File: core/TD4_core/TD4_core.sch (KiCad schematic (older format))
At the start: 0 parts

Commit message: Started refactoring
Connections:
- net labels removed: CLK, nRESET
- wire segments 61 -> 9

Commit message: RAM refactoring goes on
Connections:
- net labels added: GND, VCC
- net labels removed: 0, 1, 2, 3
- wire segments 9 -> 3
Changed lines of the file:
@@
 $EndDescr
 $Sheet
-S 1650 1200 1350 800
+S 1200 2100 1350 800
 U 5C594EF5
 F0 "Register file" 50
 F1 "register_file.sch" 50
-F2 "A" O R 3000 1300 100
-F3 "B" O R 3000 1500 100
-F4 "OUT" O R 3000 1700 100
-F5 "PC" O R 3000 1900 100
-F6 "Reg_sel" I L 1650 1900 100
-F7 "In" I L 1650 1500 100
+F2 "A" O R 2550 2200 100
+F3 "B" O R 2550 2400 100
+F4 "OUT" O R 2550 2600 100
+F5 "PC" O R 2550 2800 100
+F6 "Reg_sel" I L 1200 2800 100
+F7 "In" I L 1200 2400 100
 $EndSheet
 $Sheet
-S 8450 1900 1150 1750
+S 5950 2300 900  400
 U 5C594F14
 F0 "Adder" 50
 F1 "Adder.sch" 50
-F2 "A_0" I L 8450 2050 101
-F3 "B_0" I L 8450 3050 101
-F4 "A_1" I L 8450 2200 101
-F5 "B_1" I L 8450 3200 101
-F6 "A_2" I L 8450 2350 101
-F7 "B_2" I L 8450 3350 101
-F8 "A_3" I L 8450 2500 101
-F9 "B_3" I L 8450 3500 101
-F10 "Sum_0" I R 9600 2550 101
-F11 "Sum_1" I R 9600 2700 101
-F12 "Sum_2" I R 9600 2850 101
-F13 "Sum_3" I R 9600 3000 101
-F14 "C_out" I R 9600 3300 101
+F2 "C_out" O R 6850 2600 100
+F3 "A" I L 5950 2400 100
+F4 "B" I L 5950 2600 100
+F5 "Q" O R 6850 2400 100
 $EndSheet
 $Sheet
@@
 $EndSheet
 $Sheet
-S 5250 1250 1350 2100
+S 3750 2100 550  800
 U 5C594F9A
 F0 "Multiplexer 4x 4->1" 50
 F1 "Multiplexer_4x_4-1.sch" 50
-F2 "In_A_0" I L 5250 1350 101
-F3 "In_A_1" I L 5250 1500 101
-F4 "In_A_2" I L 5250 1650 101
-F5 "In_A_3" I L 5250 1800 101
-F6 "In_B_0" I L 5250 2050 101
-F7 "In_B_1" I L 5250 2200 101
-F8 "In_B_2" I L 5250 2350 101
-F9 "In_B_3" I L 5250 2500 101
-F10 "In_IN_0" I L 5250 2750 101
-F11 "In_IN_1" I L 5250 2900 101
-F12 "In_IN_2" I L 5250 3050 101
-F13 "In_IN_3" I L 5250 3200 101
-F14 "Sel_0" I R 6600 3050 101
-F15 "Sel_1" I R 6600 3200 101
-F16 "Out_0" I R 6600 2050 101
-F17 "Out_1" I R 6600 2200 101
-F18 "Out_2" I R 6600 2350 101
-F19 "Out_3" I R 6600 2500 101
+F2 "A" I L 3750 2200 100
+F3 "B" I L 3750 2400 100
+F4 "IN" I L 3750 2600 100
+F5 "Sel" I L 3750 2800 100
+F6 "Q" O R 4300 2400 100
 $EndSheet
 $Sheet
-S 8450 3950 1150 300
+S 7150 3150 1150 300
 U 5C5950B1
 F0 "Carry" 50
 F1 "Carry.sch" 50
-F2 "C_in" I L 8450 4100 101
-F5 "nC_out" I R 9600 4100 101
+F2 "C_in" I L 7150 3300 101
+F3 "~C_out" O R 8300 3300 100
 $EndSheet
+Wire Bus Line
+	2550 2200 3750 2200
+Wire Bus Line
+	2550 2400 3750 2400
+Wire Bus Line
+	4300 2400 5950 2400
 Wire Wire Line
-	2300 6300 2000 6300
-Entry Wire Line
-	2000 6300 1900 6400
-Entry Wire Line
-	2000 6450 1900 6550
-Entry Wire Line
-	2000 6600 1900 6700
-Entry Wire Line
-	2000 6750 1900 6850
+	6850 2600 6950 2600
 Wire Wire Line
-	2300 6450 2000 6450
+	6950 2600 6950 3300
 Wire Wire Line
-	2300 6600 2000 6600
-Wire Wire Line
-	2300 6750 2000 6750
-Text Label 2000 6300 0    50   ~ 0
-0
-Text Label 2000 6450 0    50   ~ 0
-1
-Text Label 2000 6600 0    50   ~ 0
-2
-Text Label 2000 6750 0    50   ~ 0
-3
-Wire Wire Line
-	9600 3300 9900 3300
-Wire Wire Line
-	9900 3300 9900 3800
-Wire Wire Line
-	9900 3800 8100 3800
-Wire Wire Line
-	8100 3800 8100 4100
-Wire Wire Line
-	8100 4100 8450 4100
+	6950 3300 7150 3300
+$Comp
+L power:GND #PWR?
+U 1 1 5C6E1765
+P 10600 6200
+F 0 "#PWR?" H 10600 5950 50  0001 C CNN
+F 1 "GND" H 10605 6027 50  0000 C CNN
+F 2 "" H 10600 6200 50  0001 C CNN
+F 3 "" H 10600 6200 50  0001 C CNN
+	1    10600 6200
+	1    0    0    -1
+$EndComp
+$Comp
+L power:VCC #PWR?
+U 1 1 5C6E17B1
+P 10300 6200
+F 0 "#PWR?" H 10300 6050 50  0001 C CNN
+F 1 "VCC" H 10317 6373 50  0000 C CNN
+F 2 "" H 10300 6200 50  0001 C CNN
+F 3 "" H 10300 6200 50  0001 C CNN
+	1    10300 6200
+	1    0    0    -1
+$EndComp
+$Comp
+L power:PWR_FLAG #FLG?
+U 1 1 5C6E17FD
+P 10600 6200
+F 0 "#FLG?" H 10600 6275 50  0001 C CNN
+F 1 "PWR_FLAG" H 10600 6374 50  0000 C CNN
+F 2 "" H 10600 6200 50  0001 C CNN
+F 3 "~" H 10600 6200 50  0001 C CNN
+	1    10600 6200
+	1    0    0    -1
+$EndComp
+$Comp
+L power:PWR_FLAG #FLG?
+U 1 1 5C6E180F
+P 10300 6200
+F 0 "#FLG?" H 10300 6275 50  0001 C CNN
+F 1 "PWR_FLAG" H 10300 6373 50  0000 C CNN
+F 2 "" H 10300 6200 50  0001 C CNN
+F 3 "~" H 10300 6200 50  0001 C CNN
+	1    10300 6200
+	-1   0    0    1
+$EndComp
 $EndSCHEMATC

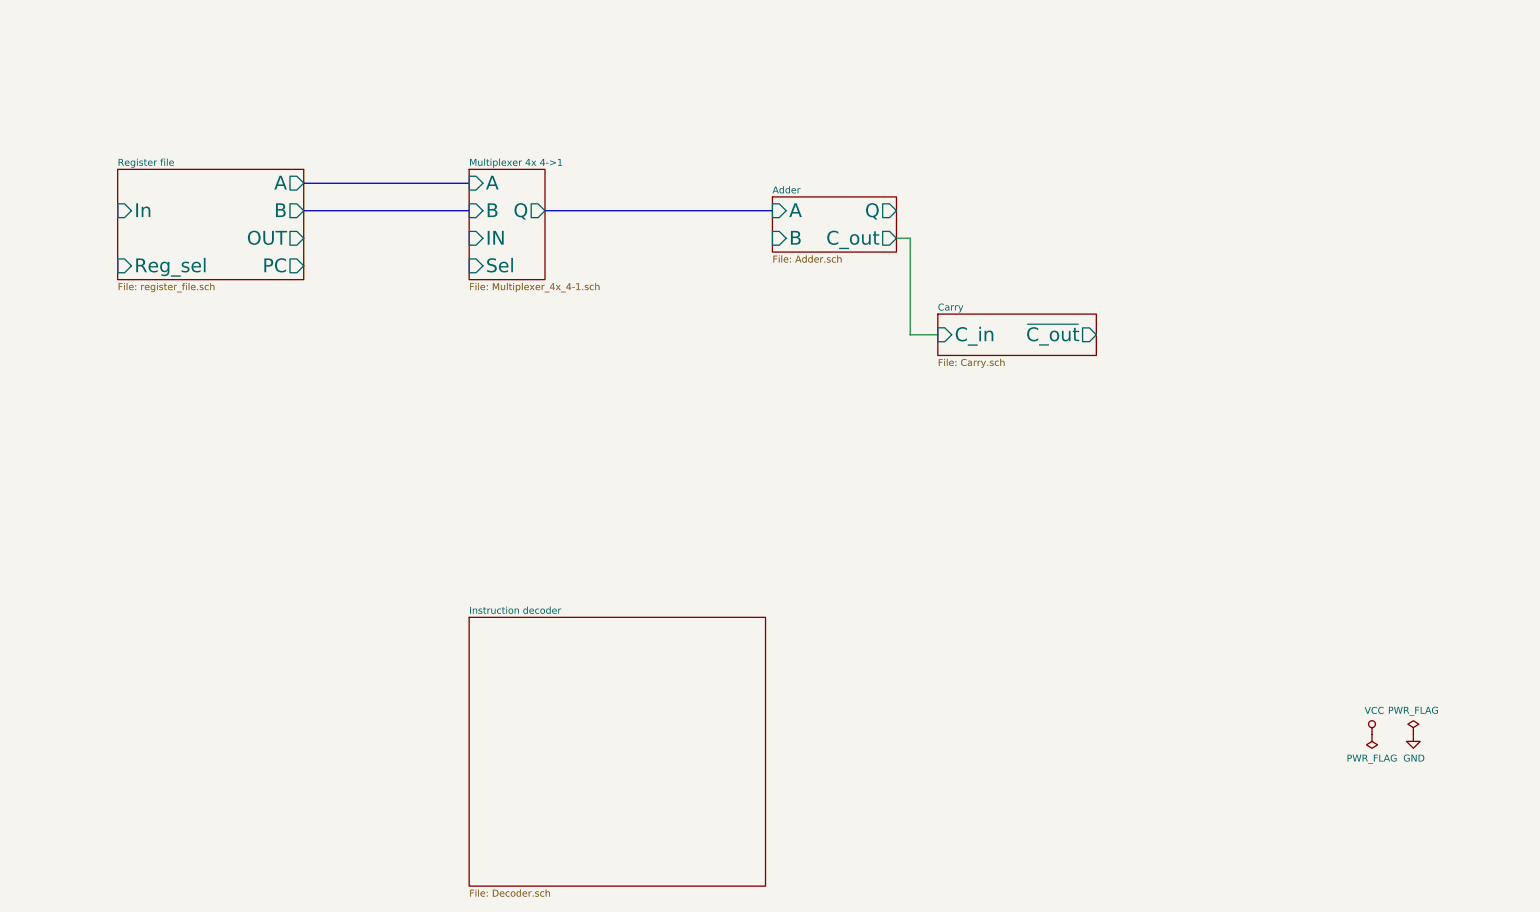
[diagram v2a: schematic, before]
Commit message: Main core schematic done; only decoder left
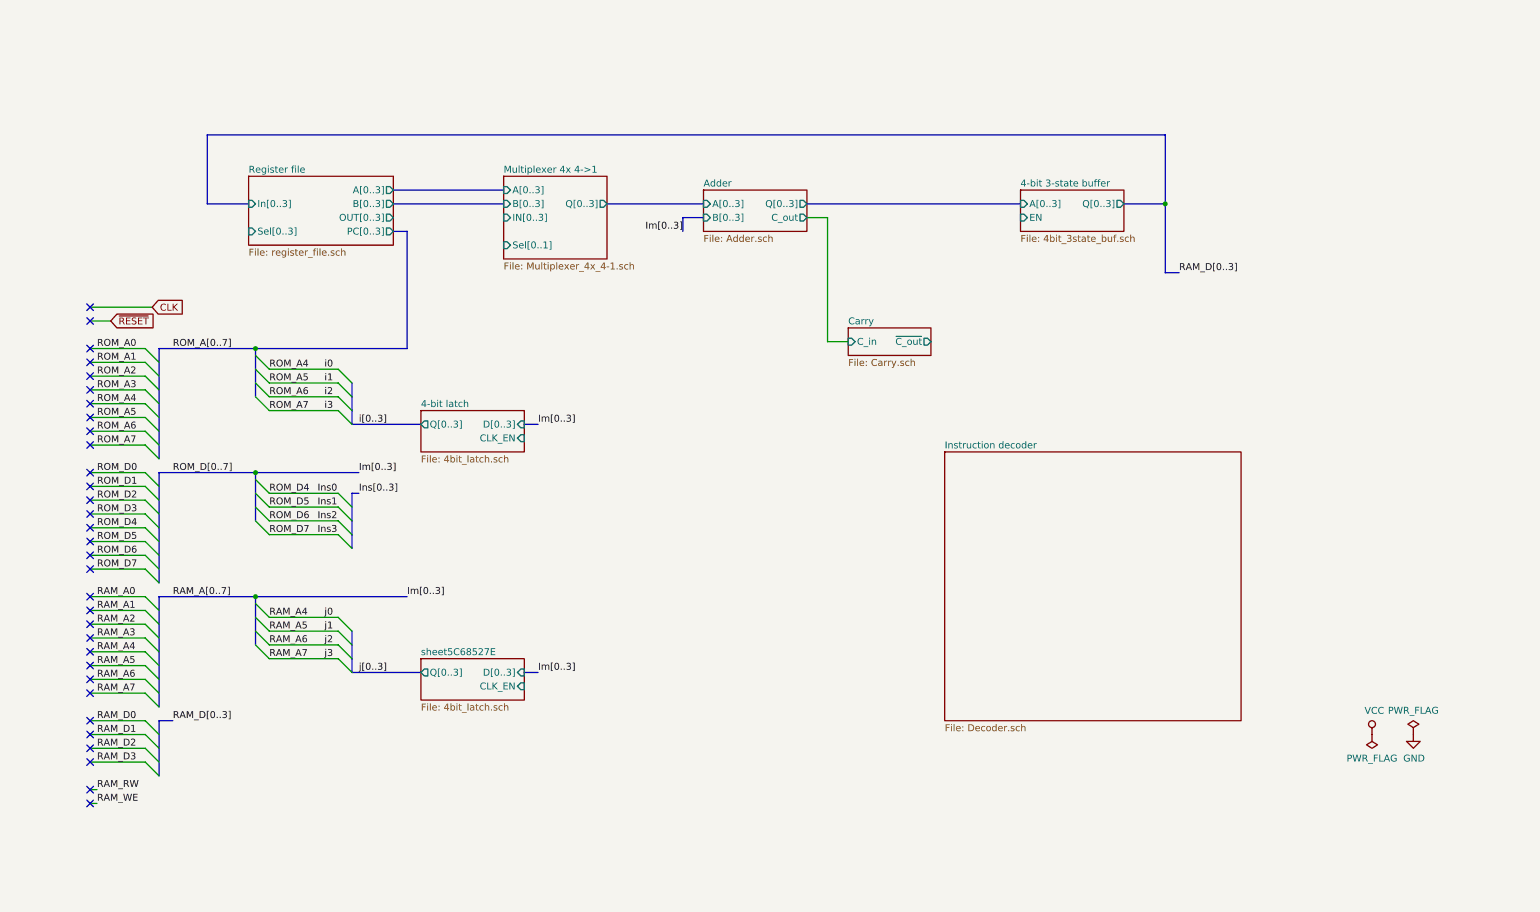
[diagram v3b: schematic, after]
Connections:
- no-connect marks 0 -> 32

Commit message: Core assembled; decoder left
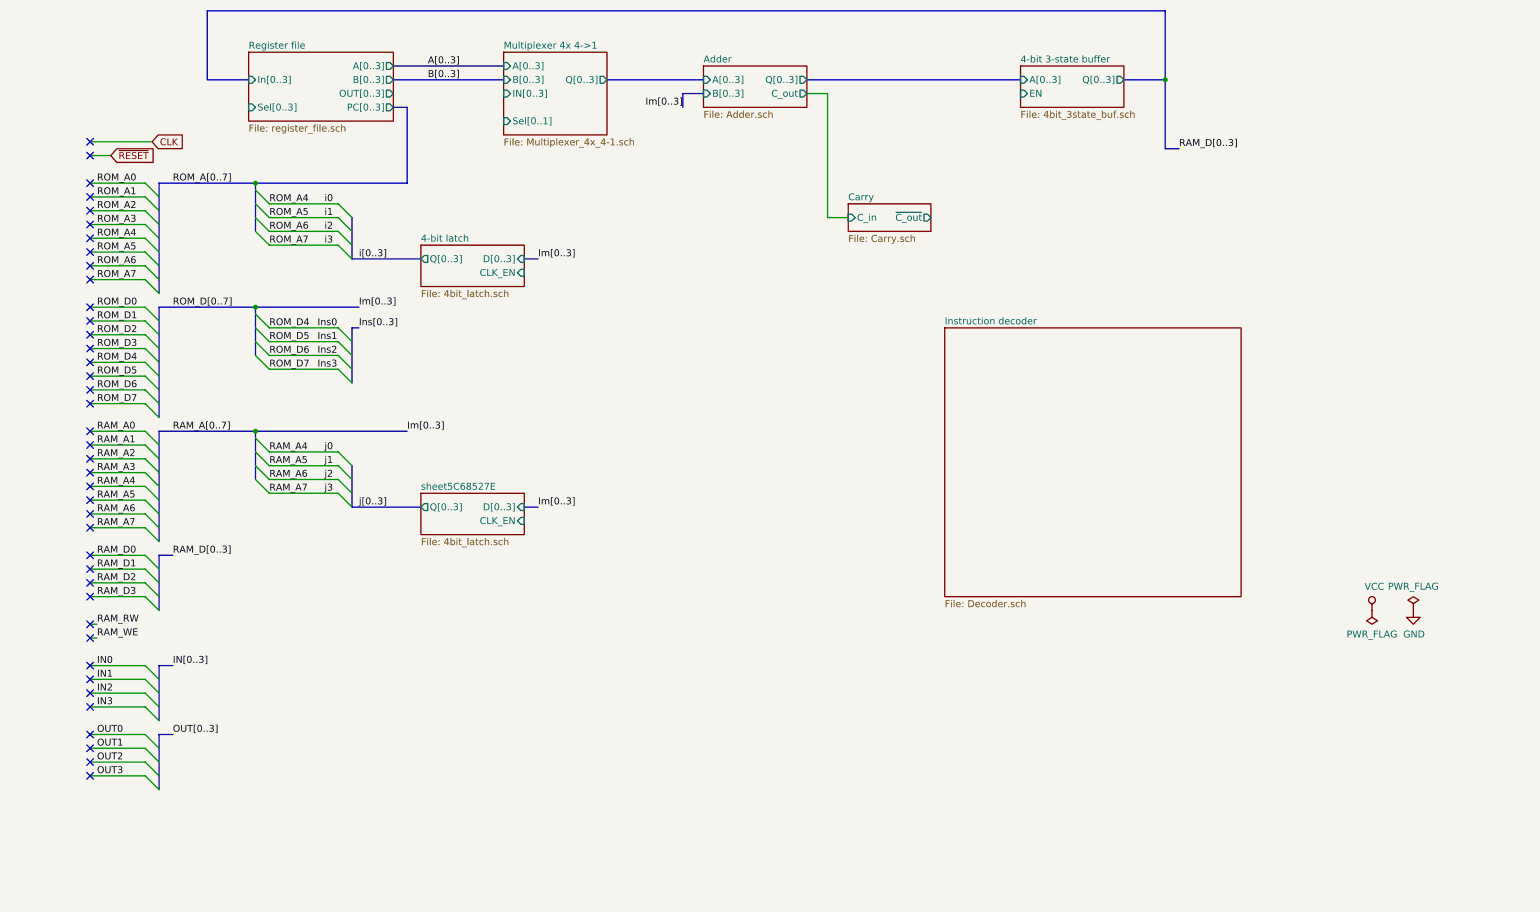
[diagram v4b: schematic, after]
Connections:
- no-connect marks 32 -> 40

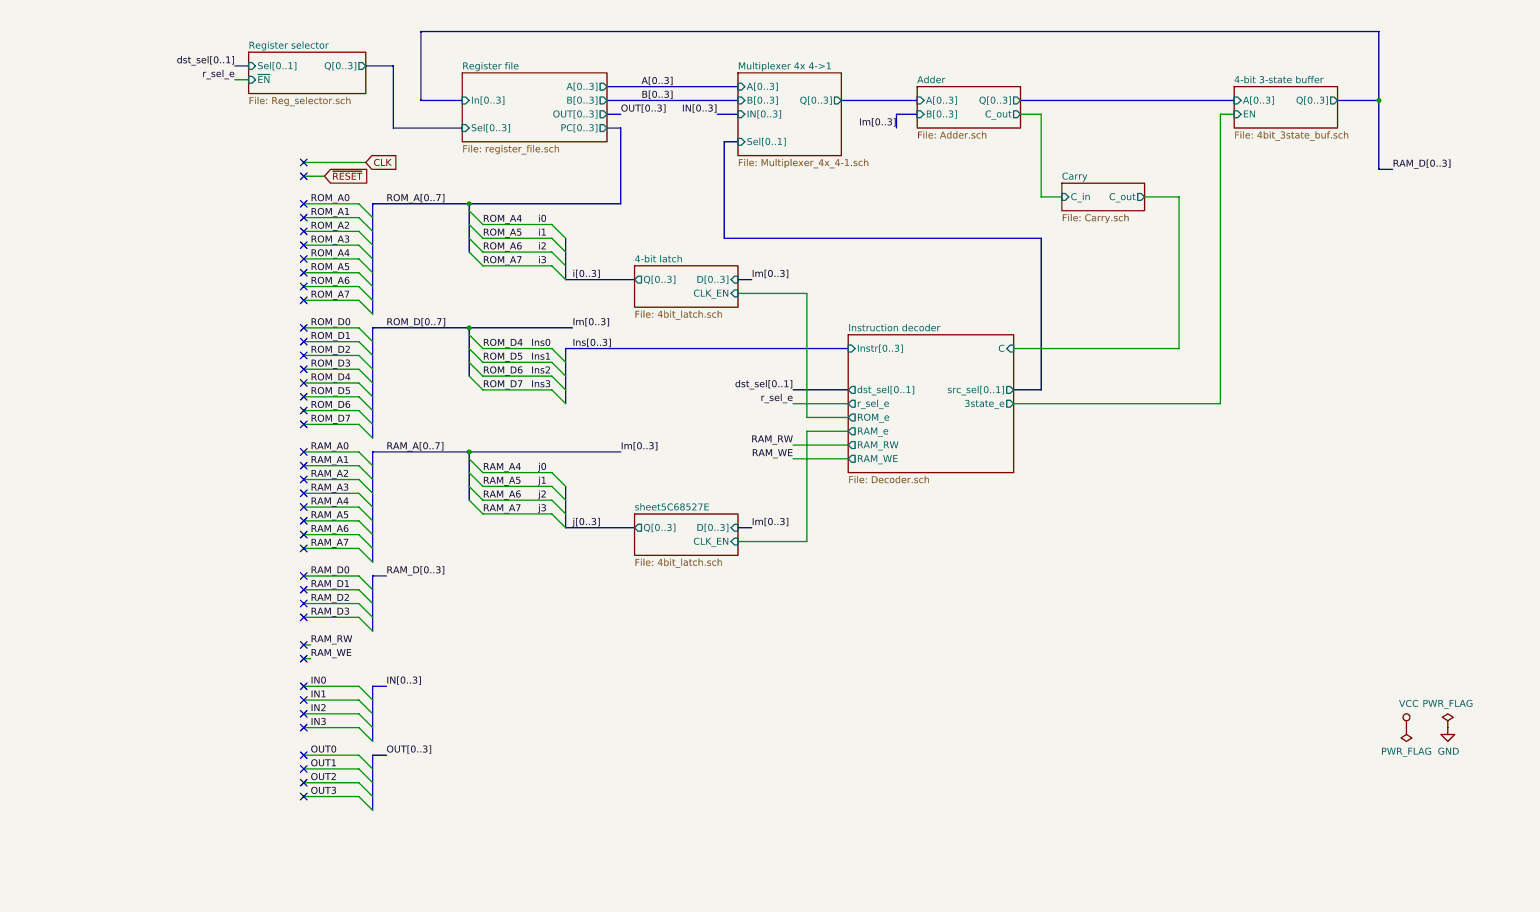
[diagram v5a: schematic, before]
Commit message: Core schematic done. Backplane connector added, including separate .sch file to append.
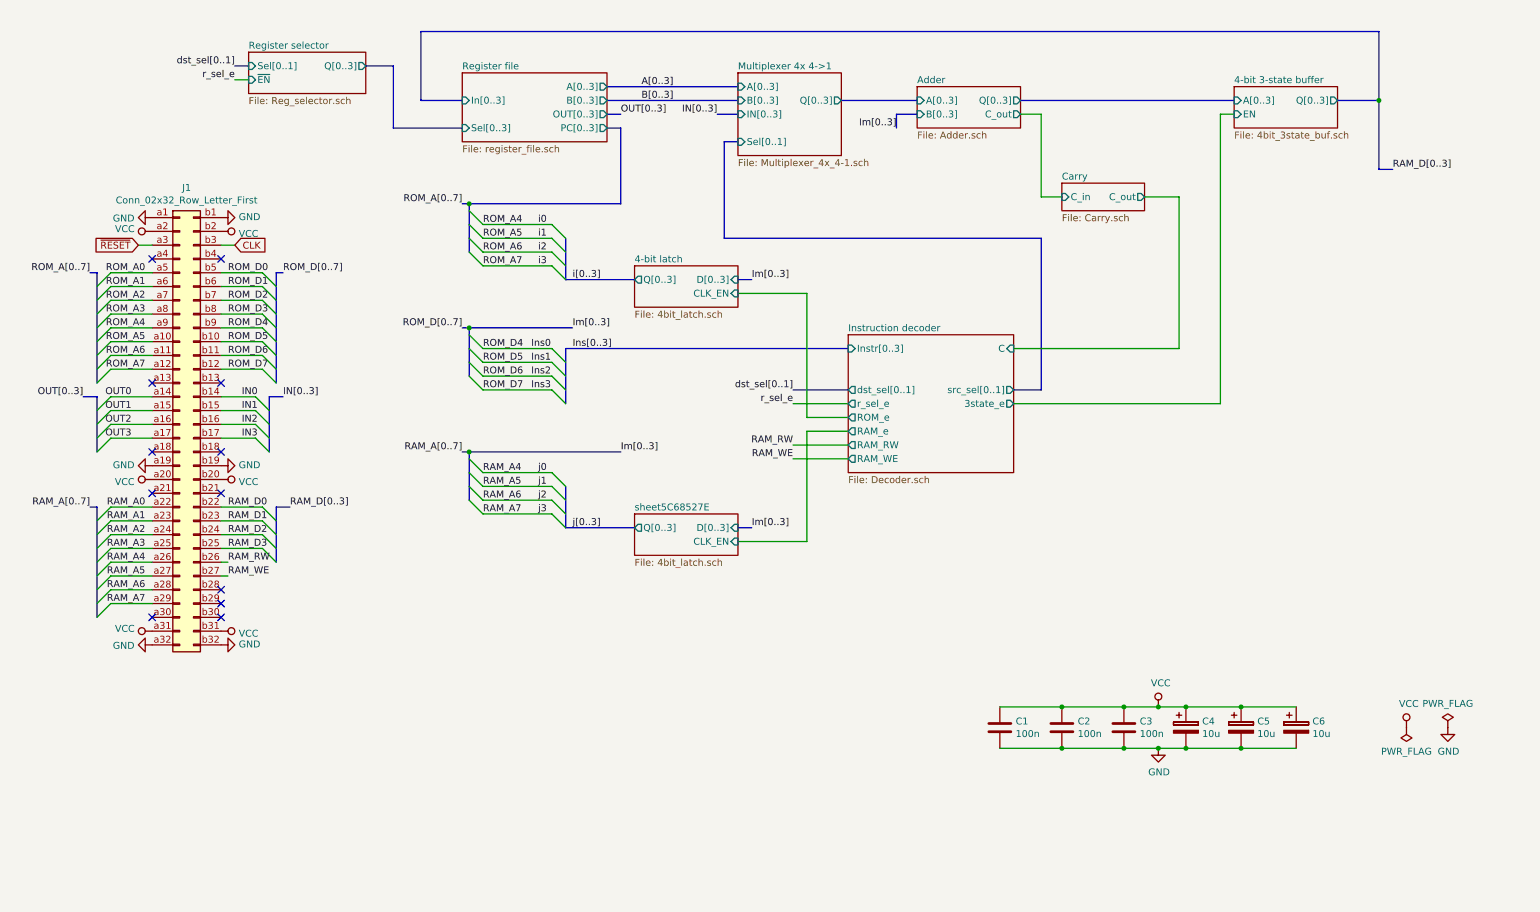
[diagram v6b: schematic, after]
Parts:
- added C1, C2, C3: 100n, Capacitor_SMD:C_0805_2012Metric, symbol Device:C
- added C4, C5, C6: 10u, Capacitor_Tantalum_SMD:CP_EIA-3216-18_Kemet-A, symbol Device:CP
- added J1: Conn_02x32_Row_Letter_First, Connector_DIN:DIN41612_B_2x32_Horizontal, symbol Connector_Generic:Conn_02x32_Row_Letter_First
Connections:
- net CLK: now also J1.b3 (Pin_b3)
- net GND: now also C1.2, C2.2, C3.2, C4.2, C5.2, C6.2, J1.a1 (Pin_a1), J1.a19 (Pin_a19), J1.a32 (Pin_a32), J1.b1 (Pin_b1), J1.b19 (Pin_b19), J1.b32 (Pin_b32)
- net IN0: now also J1.b14 (Pin_b14)
- net IN1: now also J1.b15 (Pin_b15)
- net IN2: now also J1.b16 (Pin_b16)
- net IN3: now also J1.b17 (Pin_b17)
- net Ins0: now also J1.b9 (Pin_b9)
- net Ins1: now also J1.b10 (Pin_b10)
- net Ins2: now also J1.b11 (Pin_b11)
- net Ins3: now also J1.b12 (Pin_b12)
- net OUT0: now also J1.a14 (Pin_a14)
- net OUT1: now also J1.a15 (Pin_a15)
- net OUT2: now also J1.a16 (Pin_a16)
- net OUT3: now also J1.a17 (Pin_a17)
- net RAM_A0: now also J1.a22 (Pin_a22)
- net RAM_A1: now also J1.a23 (Pin_a23)
- net RAM_A2: now also J1.a24 (Pin_a24)
- net RAM_A3: now also J1.a25 (Pin_a25)
- net RAM_A4: now also J1.a26 (Pin_a26)
- net RAM_A5: now also J1.a27 (Pin_a27)
- net RAM_A6: now also J1.a28 (Pin_a28)
- net RAM_A7: now also J1.a29 (Pin_a29)
- net RAM_D0: now also J1.b22 (Pin_b22)
- net RAM_D1: now also J1.b23 (Pin_b23)
- net RAM_D2: now also J1.b24 (Pin_b24)
- net RAM_D3: now also J1.b25 (Pin_b25)
- net RAM_RW: now also J1.b26 (Pin_b26)
- net RAM_WE: now also J1.b27 (Pin_b27)
- net ROM_A0: now also J1.a5 (Pin_a5)
- net ROM_A1: now also J1.a6 (Pin_a6)
- net ROM_A2: now also J1.a7 (Pin_a7)
- net ROM_A3: now also J1.a8 (Pin_a8)
- net ROM_A4: now also J1.a9 (Pin_a9)
- net ROM_A5: now also J1.a10 (Pin_a10)
- net ROM_A6: now also J1.a11 (Pin_a11)
- net ROM_A7: now also J1.a12 (Pin_a12)
- net ROM_D0: now also J1.b5 (Pin_b5)
- net ROM_D1: now also J1.b6 (Pin_b6)
- net ROM_D2: now also J1.b7 (Pin_b7)
- net ROM_D3: now also J1.b8 (Pin_b8)
- net VCC: now also C1.1, C2.1, C3.1, C4.1, C5.1, C6.1, J1.a2 (Pin_a2), J1.a20 (Pin_a20), J1.a31 (Pin_a31), J1.b2 (Pin_b2), J1.b20 (Pin_b20), J1.b31 (Pin_b31)
- net ~RESET: now also J1.a3 (Pin_a3)
- no-connect marks 40 -> 12
